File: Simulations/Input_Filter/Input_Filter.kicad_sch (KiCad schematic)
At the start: 18 parts, among them U21 TL072

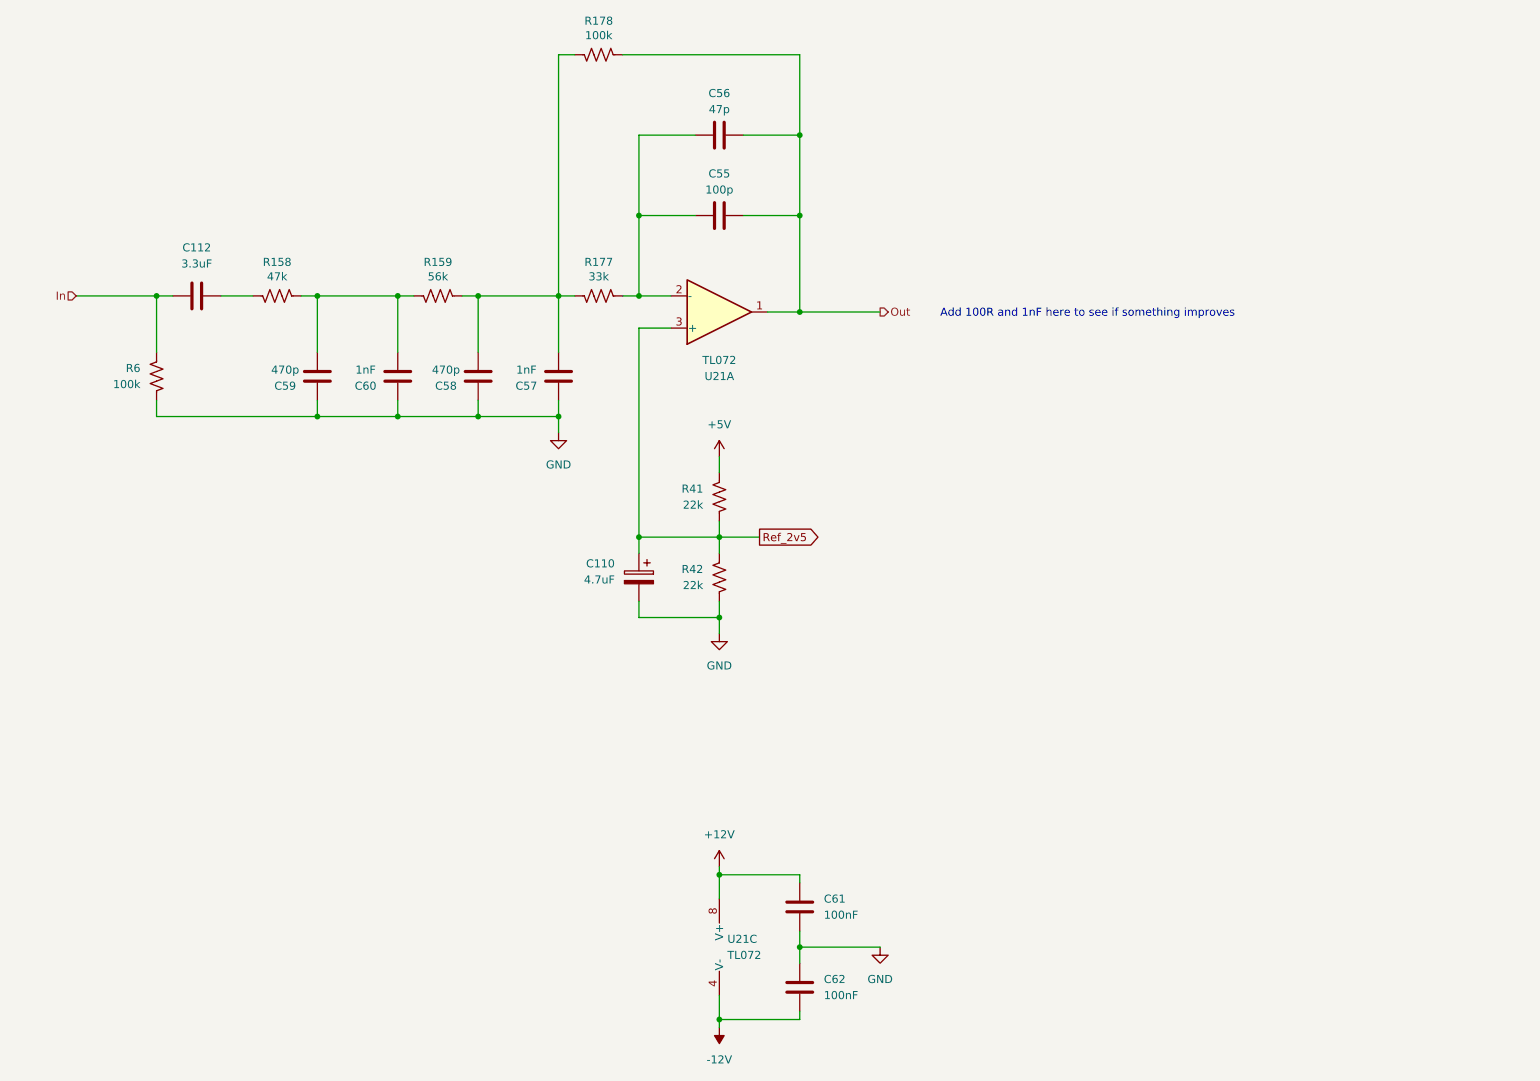
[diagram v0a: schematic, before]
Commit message: Simulated IO filters
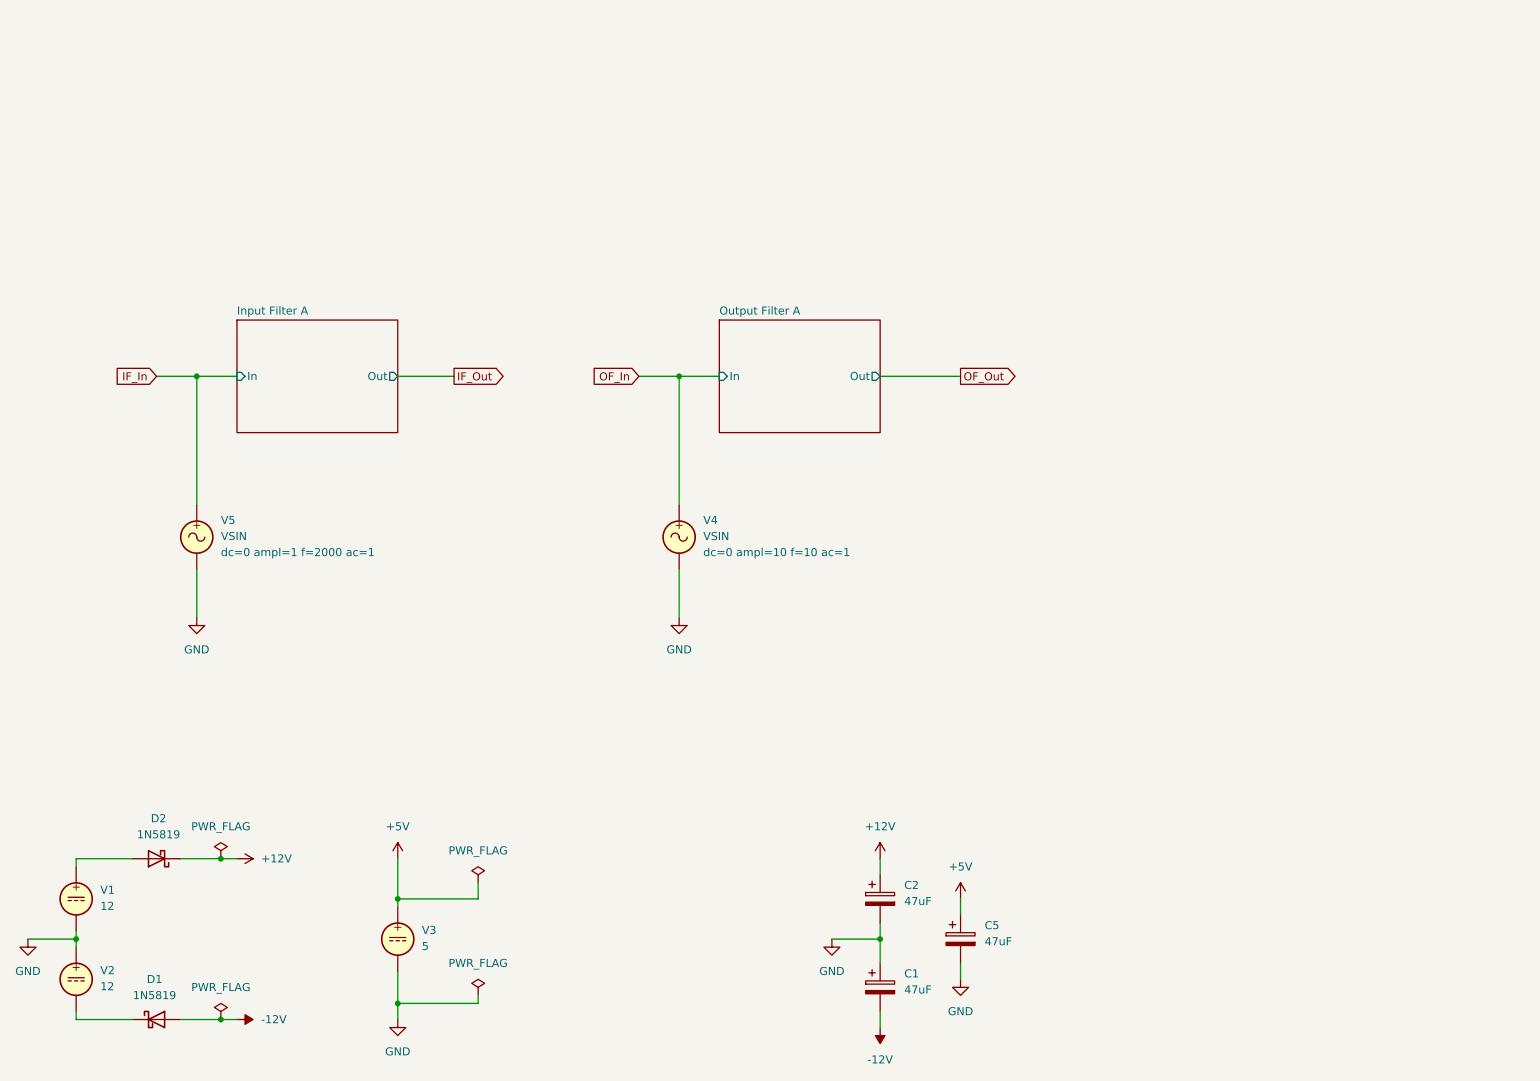
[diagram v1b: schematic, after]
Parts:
- removed C110: 4.7uF, Capacitor_THT:CP_Radial_D4.0mm_P1.50mm, symbol Device:C_Polarized
- removed C112: 3.3uF, Capacitor_THT:C_Disc_D4.3mm_W1.9mm_P5.00mm, symbol Device:C
- removed C55: 100p, Capacitor_THT:C_Disc_D3.0mm_W2.0mm_P2.50mm, symbol Device:C
- removed C56: 47p, Capacitor_THT:C_Disc_D3.0mm_W2.0mm_P2.50mm, symbol Device:C
- removed C57, C60: 1nF, Capacitor_THT:C_Disc_D3.0mm_W2.0mm_P2.50mm, symbol Device:C
- removed C58, C59: 470p, Capacitor_THT:C_Disc_D3.0mm_W2.0mm_P2.50mm, symbol Device:C
- removed C61, C62: 100nF, Capacitor_THT:C_Disc_D4.3mm_W1.9mm_P5.00mm, symbol Device:C
- removed R158: 47k, Resistor_THT:R_Axial_DIN0207_L6.3mm_D2.5mm_P7.62mm_Horizontal, symbol Device:R_US
- removed R159: 56k, Resistor_THT:R_Axial_DIN0207_L6.3mm_D2.5mm_P7.62mm_Horizontal, symbol Device:R_US
- removed R177: 33k, Resistor_THT:R_Axial_DIN0207_L6.3mm_D2.5mm_P7.62mm_Horizontal, symbol Device:R_US
- removed R178, R6: 100k, Resistor_THT:R_Axial_DIN0207_L6.3mm_D2.5mm_P7.62mm_Horizontal, symbol Device:R_US
- removed R41, R42: 22k, Resistor_THT:R_Axial_DIN0207_L6.3mm_D2.5mm_P7.62mm_Horizontal, symbol Device:R_US
- removed U21: TL072, Package_DIP:DIP-8_W7.62mm_Socket, symbol Amplifier_Operational:TL072
- added C1, C2: 47uF, Capacitor_THT:CP_Radial_D5.0mm_P2.00mm, symbol Device:C_Polarized
- added C5: 47uF, Capacitor_THT:CP_Radial_D4.0mm_P1.50mm, symbol Device:C_Polarized
- added D1, D2: 1N5819, Diode_THT:D_DO-41_SOD81_P10.16mm_Horizontal, symbol Diode:1N5819
- added V1, V2: 12, symbol Simulation_SPICE:VDC
- added V3: 5, symbol Simulation_SPICE:VDC
- added V4, V5: VSIN, symbol Simulation_SPICE:VSIN
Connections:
- net +12V: now also C2.1, D2.1 (K)
- net +5V: now also C5.1, V3.1
- net -12V: now also C1.2, D1.2 (A)
- net GND: now also C1.1, C2.2, C5.2, V1.2, V2.1, V3.2, V4.2, V5.2
- new net: D2.2 (A), V1.1
- new net: D1.1 (K), V2.2
- new net IF_In: V5.1
- new net OF_In: V4.1
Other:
- added sheet Input Filter A (Input_filter_A.kicad_sch)
- added sheet Output Filter A (Output_filter_A.kicad_sch)
- note removed: "Add 100R and 1nF here to see if something improves"

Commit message: Fixed issue with SPICE model
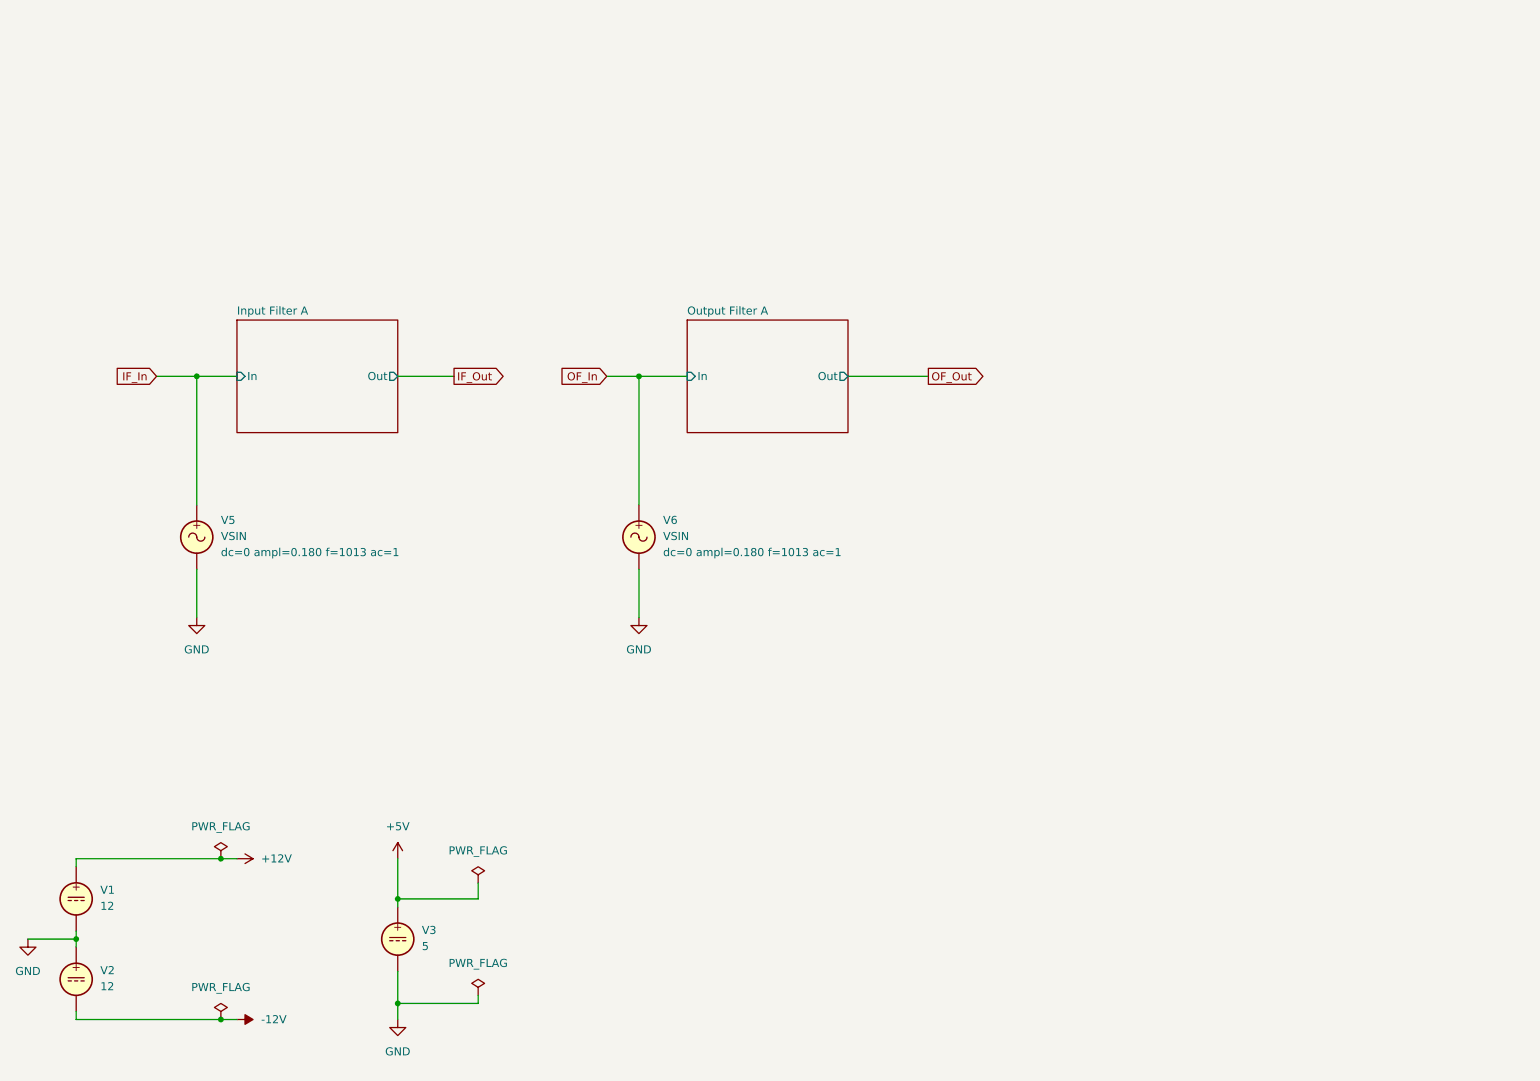
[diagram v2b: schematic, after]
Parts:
- removed C1, C2: 47uF, Capacitor_THT:CP_Radial_D5.0mm_P2.00mm, symbol Device:C_Polarized
- removed C5: 47uF, Capacitor_THT:CP_Radial_D4.0mm_P1.50mm, symbol Device:C_Polarized
- removed D1, D2: 1N5819, Diode_THT:D_DO-41_SOD81_P10.16mm_Horizontal, symbol Diode:1N5819
- removed V4: VSIN, symbol Simulation_SPICE:VSIN
- added V6: VSIN, symbol Simulation_SPICE:VSIN
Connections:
- net +12V: now also V1.1
- net -12V: now also V2.2
- net GND: now also V6.2
- net OF_In: now also V6.1

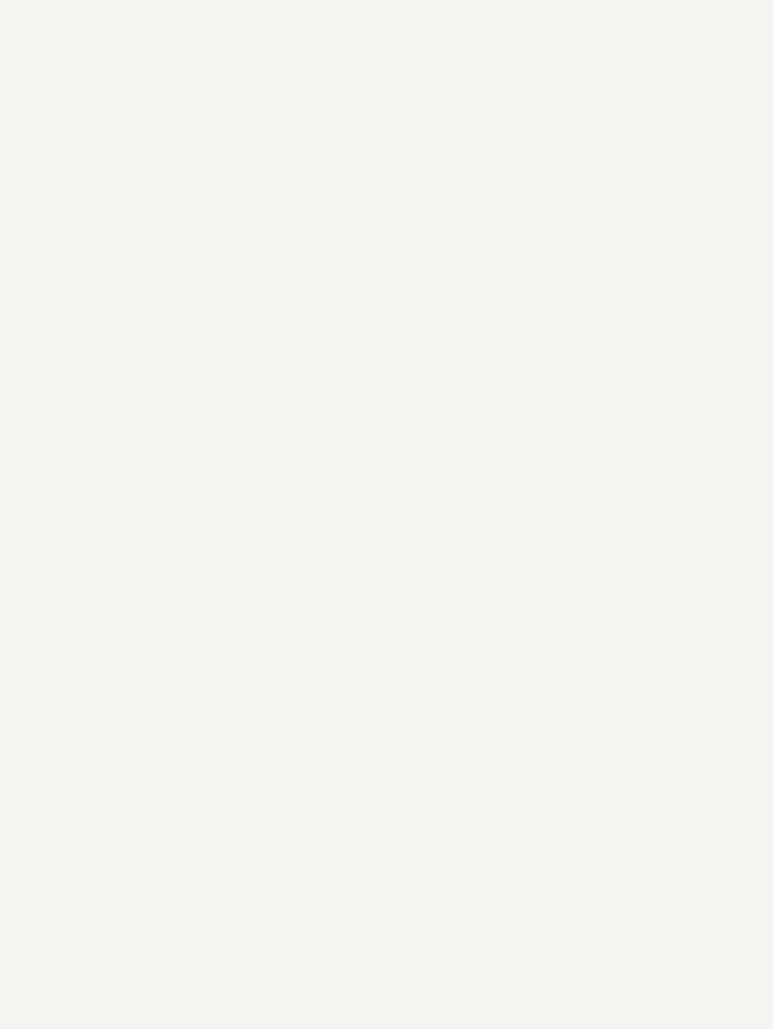
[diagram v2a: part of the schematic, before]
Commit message: Scaled up components in Tone Control part
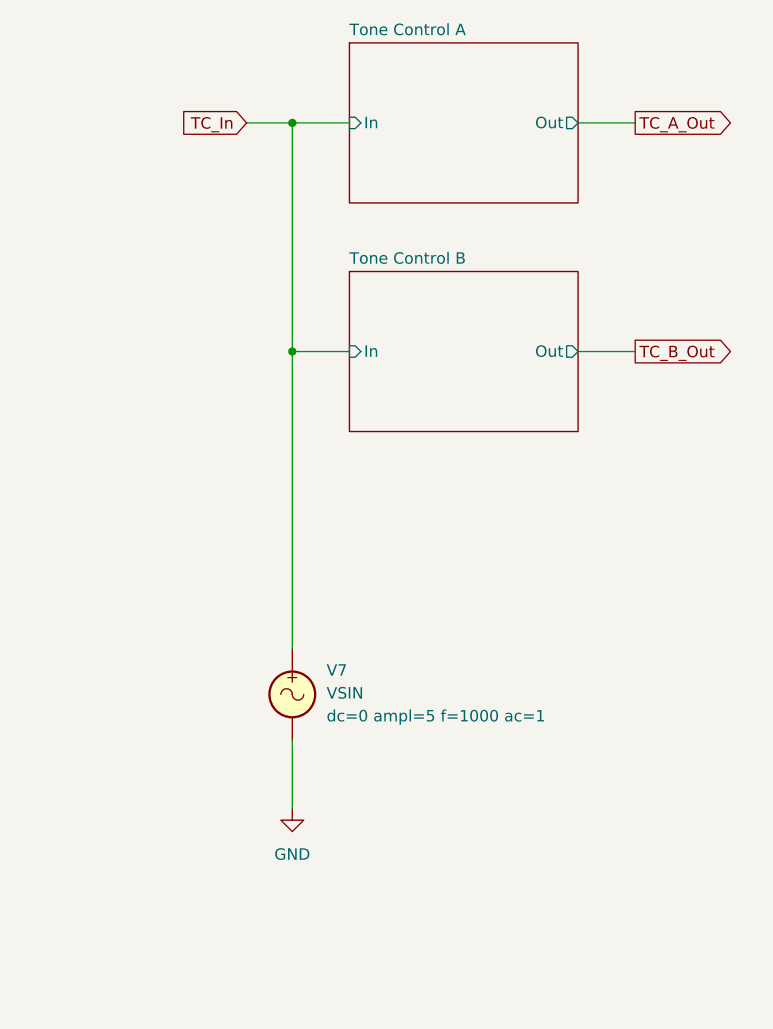
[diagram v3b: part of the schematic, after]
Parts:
- added V7: VSIN, symbol Simulation_SPICE:VSIN
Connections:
- net GND: now also V7.2
- new net TC_In: V7.1
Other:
- added sheet Tone Control A (Tone_Control_A.kicad_sch)
- added sheet Tone Control B (Tone_Control_B.kicad_sch)

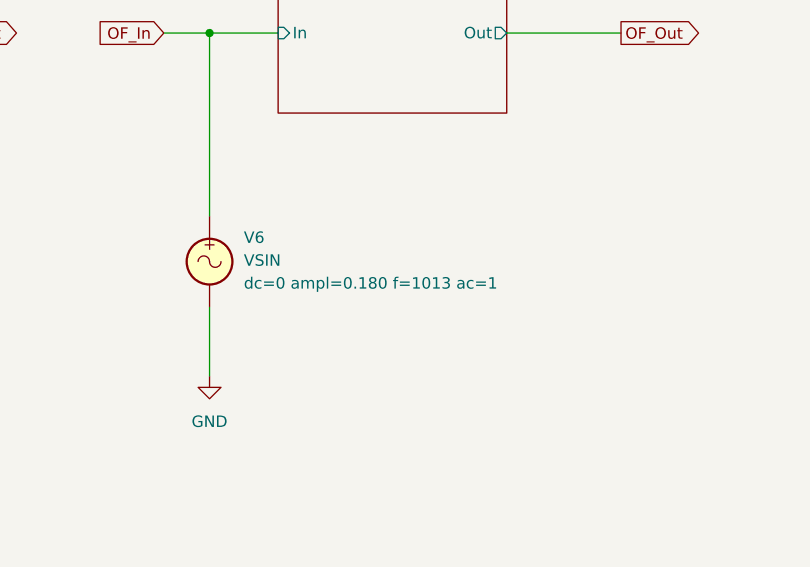
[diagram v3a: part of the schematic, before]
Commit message: Removed compander and adjusted feedback
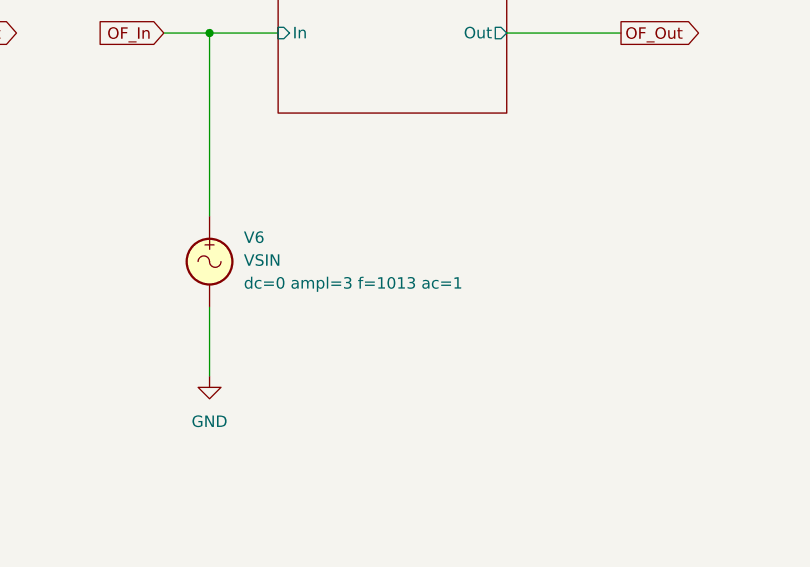
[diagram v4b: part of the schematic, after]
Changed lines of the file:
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@@
 			)
 		)
-		(property "Sim.Params" "dc=0 ampl=0.180 f=1013 ac=1"
+		(property "Sim.Params" "dc=0 ampl=3 f=1013 ac=1"
 			(at 118.11 104.0101 0)
 			(show_name no)

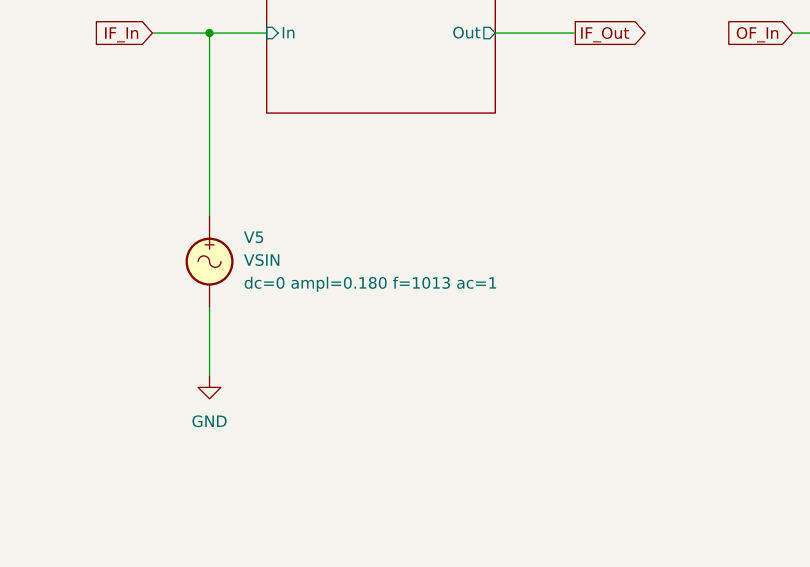
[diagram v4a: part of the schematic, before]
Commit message: Added anti-ringing RC network to IF sim
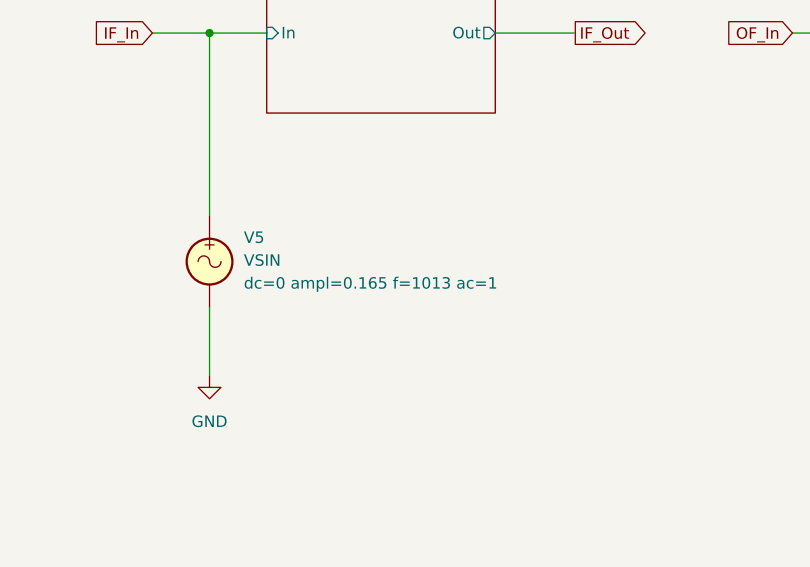
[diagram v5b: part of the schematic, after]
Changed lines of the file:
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@@
 			)
 		)
-		(property "Sim.Params" "dc=0 ampl=0.180 f=1013 ac=1"
+		(property "Sim.Params" "dc=0 ampl=0.165 f=1013 ac=1"
 			(at 48.26 104.0101 0)
 			(show_name no)
